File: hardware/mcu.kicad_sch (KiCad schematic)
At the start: 35 parts, among them J4 PROG, U16 TMP100, U6 RP2040, U9 IS25LP080D-JULE, Y1 2TJ412000NYGBC

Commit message: FEM v3 Updates
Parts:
- removed C16: 100n, Capacitor_SMD:C_0402_1005Metric, symbol Device:C
- removed TP1, TP2, TP3, TP4: TestPoint, TestPoint:TestPoint_Pad_D1.0mm, symbol Connector:TestPoint
- removed U16: TMP100, Package_TO_SOT_SMD:SOT-23-6, symbol Sensor_Temperature:TMP100
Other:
- note removed: "I2C Address - 0b1001000"

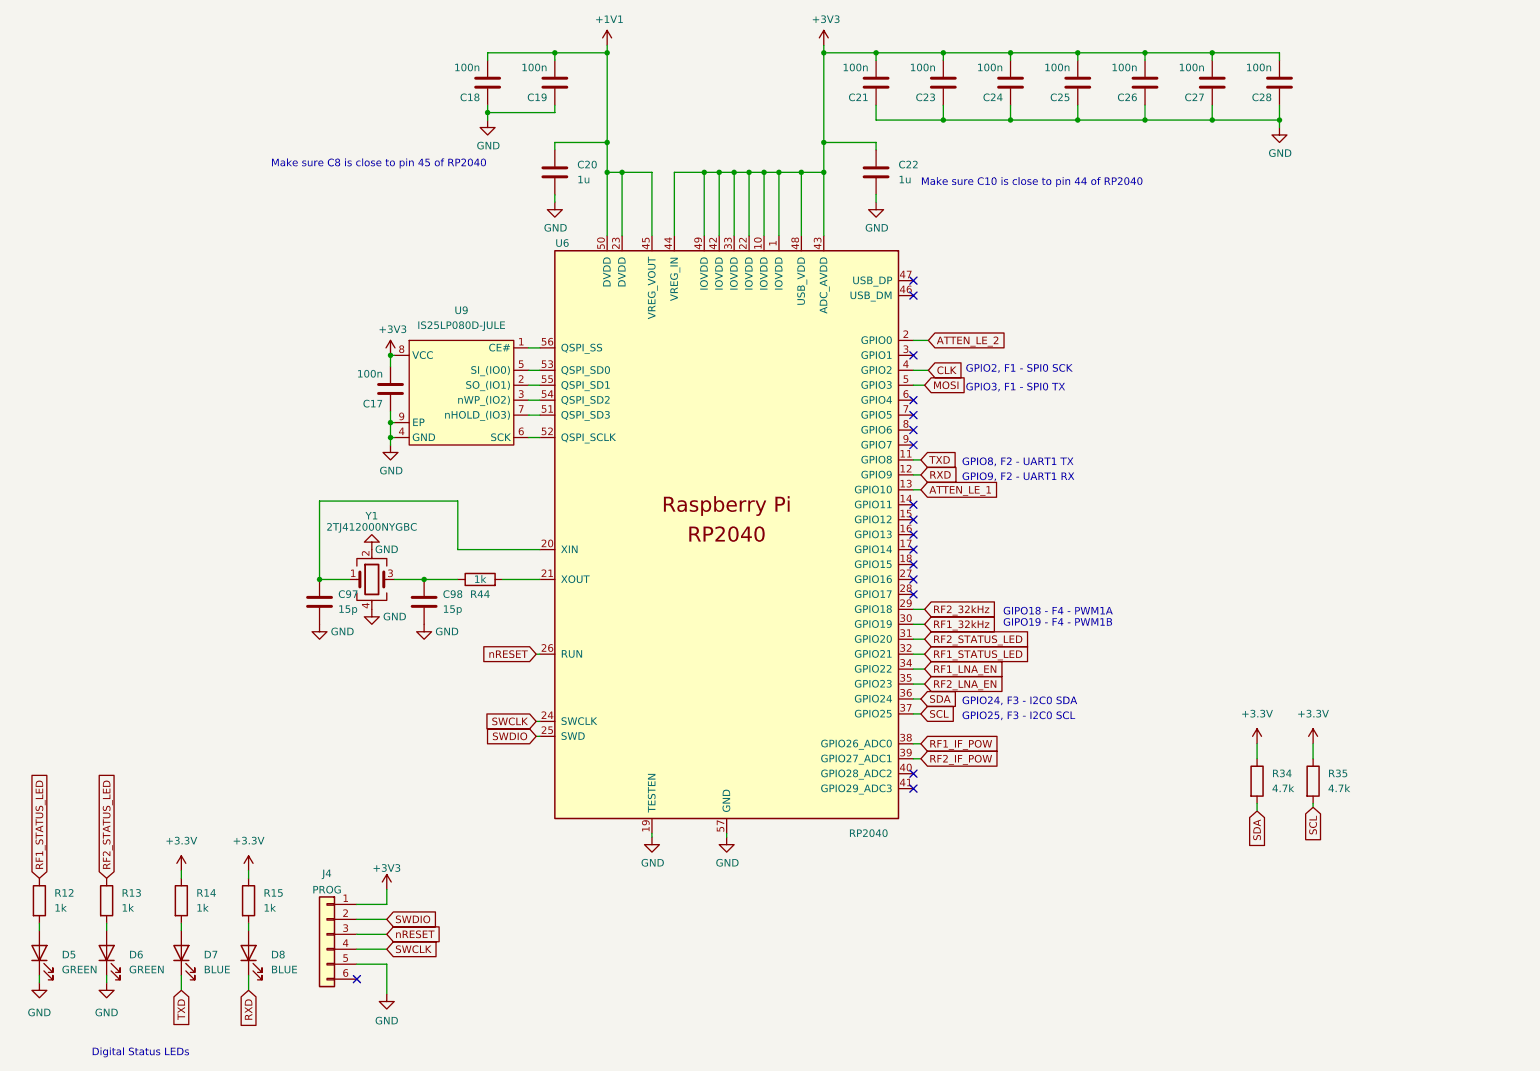
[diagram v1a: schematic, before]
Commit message: Remove cal circuit, swap attens, swap norflash
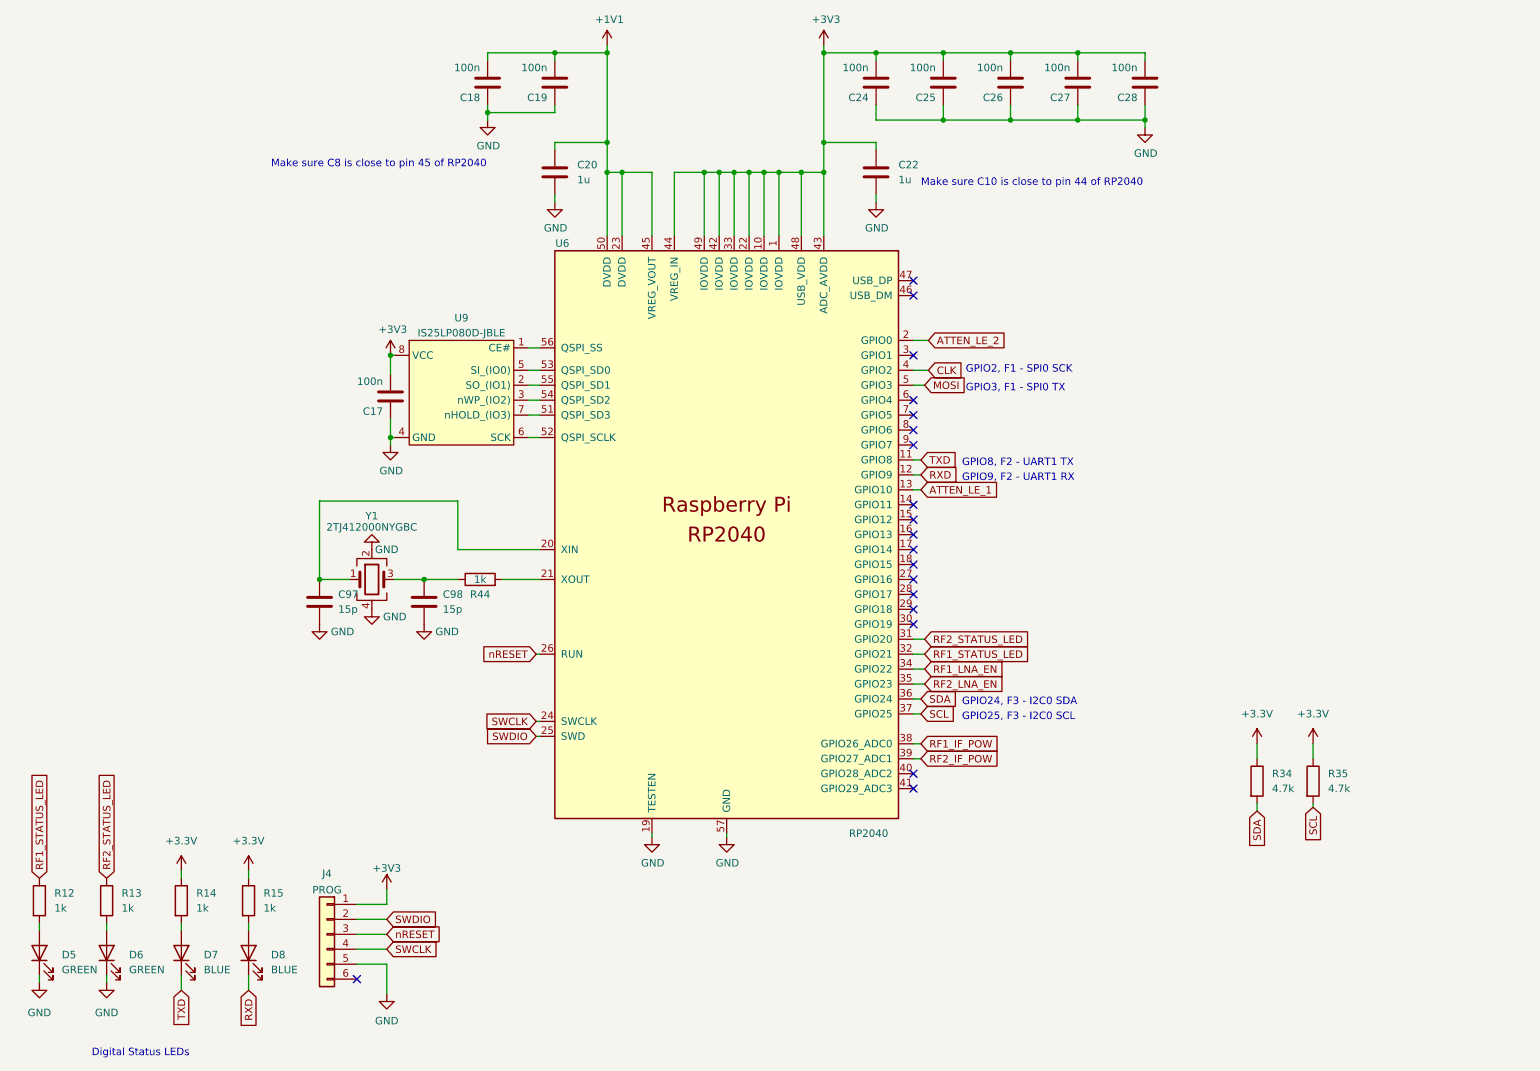
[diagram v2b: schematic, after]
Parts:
- removed C21, C23: 100n, Capacitor_SMD:C_0402_1005Metric, symbol Device:C
- removed U9: IS25LP080D-JULE, Library:USON-8-1EP_3x2mm_P0.5mm_EP0.2x1.6mm, symbol Project Library:IS25LP080D-JULE
- added U9: IS25LP080D-JBLE, Package_SO:SOIC-8_5.275x5.275mm_P1.27mm, symbol Project Library:IS25LP080D-JBLE
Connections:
- net +3V3: now also U9.8 (VCC)
- net at U6.51 (QSPI_SD3): now also U9.7 (nHOLD_(IO3))
- net at U6.52 (QSPI_SCLK): now also U9.6 (SCK)
- net at U6.53 (QSPI_SD0): now also U9.5 (SI_(IO0))
- net at U6.54 (QSPI_SD2): now also U9.3 (nWP_(IO2))
- net at U6.55 (QSPI_SD1): now also U9.2 (SO_(IO1))
- net at U6.56 (QSPI_SS): now also U9.1 (CE#)
- net GND renamed EP
- net EP: now also U9.4 (GND), U9.9 (EP)
- net RF1_32kHz: no longer names the net of U6.30 (GPIO19)
- net RF2_32kHz: no longer names the net of U6.29 (GPIO18)
- no-connect marks 17 -> 19
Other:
- note removed: "GIPO18 - F4 - PWM1A"
- note removed: "GIPO19 - F4 - PWM1B"
- moved on the sheet: C17, C24, C25, C26, C27, C28

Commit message: Fix BOM errors
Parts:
- R34, R35: LCSC C138060 -> C137962; MPN RC0402FR-0712K4L -> RC0402FR-074R7L
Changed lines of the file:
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@@
       (effects (font (size 1.27 1.27)) hide)
     )
-    (property "LCSC" "C138060" (at 236.855 149.86 0)
+    (property "LCSC" "C137962" (at 236.855 149.86 0)
       (effects (font (size 1.27 1.27)) hide)
     )
-    (property "MPN" "RC0402FR-0712K4L" (at 236.855 149.86 0)
+    (property "MPN" "RC0402FR-074R7L" (at 236.855 149.86 0)
       (effects (font (size 1.27 1.27)) hide)
     )
@@
       (effects (font (size 1.27 1.27)) hide)
     )
-    (property "LCSC" "C138060" (at 227.33 149.86 0)
+    (property "LCSC" "C137962" (at 227.33 149.86 0)
       (effects (font (size 1.27 1.27)) hide)
     )
-    (property "MPN" "RC0402FR-0712K4L" (at 227.33 149.86 0)
+    (property "MPN" "RC0402FR-074R7L" (at 227.33 149.86 0)
       (effects (font (size 1.27 1.27)) hide)
     )
